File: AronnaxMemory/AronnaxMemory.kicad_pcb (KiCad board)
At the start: 6 copper layers, 152.4 x 64.8 mm, 41 parts, among them J1 Barrel_Jack_Switch, J2 Conn_02x40_Odd_Even, J3 Conn_02x18_Odd_Even, J5 I/O, J8 Conn_02x40_Odd_Even, U1 W65C22SxP, U10 ATF22V10, U11 W65C51NxP, U12 MAX232, U2 MAX232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

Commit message: All of it
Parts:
- removed J5: I/O, Connector_PinHeader_2.54mm:PinHeader_2x09_P2.54mm_Vertical
- removed U1: W65C22SxP, Package_LCC:PLCC-44_THT-Socket
- removed U11, U3: W65C51NxP, Package_LCC:PLCC-32_THT-Socket
- removed U12, U2: MAX232, Package_DIP:DIP-16_W7.62mm_Socket
- removed U6: AS6C4008-55PCN, Package_DIP:DIP-32_W15.24mm_Socket
- removed U7: AT28C256-15PU, Package_LCC:PLCC-32_THT-Socket
- removed U8: ATF22V10, Package_DIP:DIP-24_W7.62mm_Socket
- removed X2: 28MHz, Oscillator:Oscillator_DIP-8
- added C11: 100nF, Capacitor_THT:C_Disc_D3.4mm_W2.1mm_P2.50mm, F.Cu at (57.9, 113.2)
- added C12: 100nF, Capacitor_THT:C_Disc_D3.4mm_W2.1mm_P2.50mm, F.Cu at (65.8, 120.1)
- added J12: Conn_02x08_Odd_Even, Connector_PinHeader_2.54mm:PinHeader_2x08_P2.54mm_Vertical, F.Cu at (164.7, 85.7)
- added J9: VP A1-A4, Connector_PinHeader_2.54mm:PinHeader_2x04_P2.54mm_Vertical, F.Cu at (144.9, 111.3)
- J8: value Conn_02x40_Odd_Even -> Conn_02x10_Odd_Even; footprint Connector_PinHeader_2.54mm:PinHeader_2x40_P2.54mm_Vertical -> Connector_PinHeader_2.54mm:PinHeader_2x10_P2.54mm_Vertical
- moved C8 92.8 mm to (53.2, 110.9)
- moved C6 58.7 mm to (47.0, 86.4), turned to 0 degrees
- moved C10 56.9 mm to (71.9, 113.9), turned to 180 degrees
- moved J8 56.0 mm to (98.3, 107.6)
- moved U10 54.3 mm to (75.4, 122.0)
- moved C9 49.6 mm to (106.3, 115.6)
- moved U9 49.6 mm to (109.2, 123.2)
- moved C7 49.1 mm to (67.4, 100.7)
- moved C2 34.8 mm to (62.0, 107.9), turned to 90 degrees
- moved C1 20.4 mm to (39.8, 107.0), turned to 180 degrees
- moved D3 18.8 mm to (141.9, 96.6), turned to -90 degrees
- moved RN1 18.3 mm to (167.0, 93.1)
- moved C5 15.9 mm to (143.9, 93.6), turned to 180 degrees
- moved R14 15.6 mm to (144.9, 104.3)
- moved R3 15.6 mm to (169.5, 96.9)
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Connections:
- net Net-(D3-K) renamed /~{IRQV}
- J2 pad 35: R~{W} -> /R~{W}
- J2 pad 39: ~{WR} -> /~{WR}
- J3 pad 11: /AA4 -> /A4
- J3 pad 13: /AA3 -> /A3
- J3 pad 15: /AA2 -> /A2
- J3 pad 17: /AA1 -> /A1
- J8 pad 10: /AA4 -> ~{MEG6}
- J8 pad 14: ~{MEG0} -> ~{MEG8}
- J8 pad 16: ~{MEG2} -> ~{MEGA}
- J8 pad 18: ~{MEG4} -> ~{MEGC}
- J8 pad 2: ~{IRQ7} -> ~{RAM_OE}
- J8 pad 20: ~{MEG6} -> ~{MEGE}
- J8 pad 4: /AA1 -> ~{MEG0}
- J8 pad 6: /AA2 -> ~{MEG2}
- J8 pad 8: /AA3 -> ~{MEG4}
- U4 pad 2: /A1 -> /A4
- U4 pad 3: /A2 -> /A3
- U4 pad 4: /A3 -> /A2
- U4 pad 5: /A4 -> /A1
- U9 pad 1: unconnected-(U9-CLK-Pad1) -> E
- U9 pad 11: E -> /A7
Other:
- board text added: "~{CLK}"
- board text removed: "~{CLK"

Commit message: All of it p2
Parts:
- removed C10, C11, C12, C8, C9: 100nF, Capacitor_THT:C_Disc_D3.4mm_W2.1mm_P2.50mm
- removed U10, U9: ATF22V10, Package_DIP:DIP-24_W7.62mm_Socket
- added J11: Conn_02x18_Odd_Even, PCB_Edge_Connectors:PCB_Edge_36pin, B.Cu at (187.5, 100.3)
- added R13: 3.3k, Resistor_THT:R_Axial_DIN0207_L6.3mm_D2.5mm_P7.62mm_Horizontal, F.Cu at (86.2, 158.2)
- added U13: 74HC74, Package_DIP:DIP-14_W7.62mm, F.Cu at (55.9, 96.5)
- added U2: ATF22V10, Package_DIP:DIP-24_W7.62mm_Socket, F.Cu at (109.2, 119.4)
- added U3: ATF22V10, Package_DIP:DIP-24_W7.62mm_Socket, F.Cu at (76.2, 109.2)
- added U6: 74LS348, Package_DIP:DIP-16_W7.62mm_Socket, F.Cu at (142.2, 99.1)
- added U7: ATF22V10, Package_DIP:DIP-24_W7.62mm_Socket, F.Cu at (134.6, 111.8)
- added X1: 16MHz, Oscillator:Oscillator_DIP-8, F.Cu at (41.9, 118.1)
- J12: value Conn_02x08_Odd_Even -> IRQ In
- J8: value Conn_02x10_Odd_Even -> 2MB Select; footprint Connector_PinHeader_2.54mm:PinHeader_2x10_P2.54mm_Vertical -> Connector_PinHeader_2.54mm:PinHeader_2x09_P2.54mm_Vertical
- U4: value ATF22V10 -> 74AHCT32; footprint Package_DIP:DIP-24_W7.62mm_Socket -> Package_DIP:DIP-14_W7.62mm_Socket
- U5: value 74LS348 -> 74HC74; footprint Package_DIP:DIP-16_W7.62mm_Socket -> Package_DIP:DIP-14_W7.62mm
- moved C4 36.4 mm to (113.7, 92.7)
- moved U4 36.4 mm to (116.8, 97.8)
- moved C5 17.3 mm to (141.7, 76.5)
- moved D3 17.3 mm to (139.7, 79.5)
- moved R14 17.3 mm to (142.7, 87.1)
- moved R4 17.3 mm to (170.7, 79.8)
- moved J12 17.3 mm to (162.6, 68.6)
- moved R3 17.3 mm to (167.4, 79.8)
- moved R5 17.3 mm to (174.0, 79.8)
- moved RN1 17.3 mm to (164.8, 75.9)
- moved U5 17.3 mm to (146.1, 87.1)
- moved C6 11.3 mm to (41.2, 96.0)
- moved J8 9.30 mm to (99.1, 116.8)
- moved J9 8.13 mm to (144.8, 119.4)
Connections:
- net ~{RST} renamed /~{RST}
- J12 pad 10: ~{IRQ3} -> /~{IRQ3}
- J12 pad 12: ~{IRQ2} -> /~{IRQ2}
- J12 pad 14: ~{IRQ1} -> /~{IRQ1}
- J12 pad 16: ~{IRQ0} -> /~{IRQ0}
- J12 pad 2: ~{IRQ7} -> /~{IRQ7}
- J12 pad 4: ~{IRQ6} -> /~{IRQ6}
- J12 pad 6: ~{IRQ5} -> /~{IRQ5}
- J12 pad 8: ~{IRQ4} -> /~{IRQ4}
- J2 pad 11: ~{CLK_EN} -> /~{CLK_EN}
- J2 pad 15: /CLK -> unconnected-(J2-Pin_15-Pad15)
- J2 pad 17: /~{CLK} -> unconnected-(J2-Pin_17-Pad17)
- J2 pad 23: /~{ABORT} -> unconnected-(J2-Pin_23-Pad23)
- J2 pad 25: /BE -> unconnected-(J2-Pin_25-Pad25)
- J2 pad 27: /RDY_IN -> unconnected-(J2-Pin_27-Pad27)
- J2 pad 29: /~{WAI} -> unconnected-(J2-Pin_29-Pad29)
- J2 pad 31: /SYNC -> unconnected-(J2-Pin_31-Pad31)
- J2 pad 33: /VA -> unconnected-(J2-Pin_33-Pad33)
- J2 pad 41: ~{BANK0} -> /~{BANK0}
- J2 pad 43: E -> /E
- J2 pad 45: /M -> unconnected-(J2-Pin_45-Pad45)
- J2 pad 47: /X -> unconnected-(J2-Pin_47-Pad47)
- J2 pad 5: /~{MR}⎒ -> unconnected-(J2-Pin_5-Pad5)
- J2 pad 51: /~{ML} -> unconnected-(J2-Pin_51-Pad51)
- J2 pad 9: /RST -> unconnected-(J2-Pin_9-Pad9)
- J8 pad 10: ~{MEG6} -> /~{MEG8}
- J8 pad 12: ~{RAM_OE} -> /~{MEGA}
- J8 pad 14: ~{MEG8} -> /~{MEGC}
- J8 pad 16: ~{MEGA} -> /~{MEGE}
- J8 pad 18: ~{MEGC} -> ~{RAM_OE}
- J8 pad 2: ~{RAM_OE} -> /~{MEG0}
- J8 pad 4: ~{MEG0} -> /~{MEG2}
- J8 pad 6: ~{MEG2} -> /~{MEG4}
- J8 pad 8: ~{MEG4} -> /~{MEG6}
- J9 pad 2: GND -> Net-(J9-Pin_2)
- J9 pad 4: GND -> Net-(J9-Pin_2)
- J9 pad 6: GND -> Net-(J9-Pin_2)
- J9 pad 8: GND -> Net-(J9-Pin_2)
- RN1 pad 2: ~{IRQ7} -> /~{IRQ7}
- RN1 pad 3: ~{IRQ6} -> /~{IRQ6}
- RN1 pad 4: ~{IRQ5} -> /~{IRQ5}
- RN1 pad 5: ~{IRQ4} -> /~{IRQ4}
- RN1 pad 6: ~{IRQ3} -> /~{IRQ3}
- RN1 pad 7: ~{IRQ2} -> /~{IRQ2}
- RN1 pad 8: ~{IRQ1} -> /~{IRQ1}
- RN1 pad 9: ~{IRQ0} -> /~{IRQ0}
- U4 pad 1: unconnected-(U4-CLK-Pad1) -> GND
- U4 pad 10: /~{VP} -> Net-(U4-Pad10)
- U4 pad 11: unconnected-(U4-I-Pad11) -> Net-(U4-Pad10)
- U4 pad 12: GND -> /8MHz
- U4 pad 13: unconnected-(U4-I-Pad13) -> GND
- U4 pad 14: unconnected-(U4-O-Pad14) -> VCC
- U4 pad 2: /A4 -> GND
- U4 pad 3: /A3 -> unconnected-(U4-Pad3)
- U4 pad 4: /A2 -> /IOWAIT
- U4 pad 5: /A1 -> /8MHz
- U4 pad 6: unconnected-(U4-I-Pad6) -> /CLK_SRC
- U4 pad 7: /ADDEND_AA1 -> GND
- U4 pad 8: /ADDEND_AA2 -> /DCLK
- U4 pad 9: /ADDEND_AA3 -> GND
- U5 pad 1: ~{IRQ0} -> VCC
- U5 pad 10: ~{IRQ7} -> VCC
- U5 pad 11: ~{IRQ6} -> /DCLK
- U5 pad 12: ~{IRQ5} -> /STRETCH
- U5 pad 13: ~{IRQ4} -> /~{RDYRESET}
- U5 pad 14: /~{IRQV} -> VCC
- U5 pad 2: ~{IRQ1} -> /~{IOREADY}
- U5 pad 3: ~{IRQ2} -> /DCLK
- U5 pad 4: ~{IRQ3} -> /IOWAIT
- U5 pad 5: GND -> /~{RDYRESET}
- U5 pad 6: /ADDEND_AA3 -> unconnected-(U5A-~{Q}-Pad6)
- U5 pad 7: /ADDEND_AA2 -> GND
- U5 pad 8: GND -> unconnected-(U5B-~{Q}-Pad8)
- U5 pad 9: /ADDEND_AA1 -> /IOWAIT
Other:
- board size 152.4 x 64.8 mm -> 161.3 x 64.8 mm

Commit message: All of it.
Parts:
- removed D3: 1N4148, Diode_THT:D_DO-35_SOD27_P7.62mm_Horizontal
- removed R14: 10K, Resistor_THT:R_Axial_DIN0207_L6.3mm_D2.5mm_P7.62mm_Horizontal
- added D4: 1N4148, Diode_THT:D_DO-35_SOD27_P7.62mm_Horizontal, F.Cu at (51.4, 114.3)
- added R15: 10K, Resistor_THT:R_Axial_DIN0207_L6.3mm_D2.5mm_P7.62mm_Horizontal, F.Cu at (51.4, 118.1)
- moved R13 69.1 mm to (94.0, 89.5)
- moved C5 2.58 mm to (142.9, 78.8), turned to -90 degrees
- moved J12 0.64 mm to (162.6, 67.9)
- moved R3 0.64 mm to (167.4, 79.1)
- moved R4 0.64 mm to (170.7, 79.1)
- moved R5 0.64 mm to (174.0, 79.1)
- moved RN1 0.64 mm to (164.8, 75.3)
- moved U5 0.64 mm to (146.1, 86.5)
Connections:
- J11 pad 13: GND2 -> GND
- J11 pad 19: GND2 -> GND
- J11 pad 25: GND2 -> GND
- J11 pad 29: VDD -> VCC
- J11 pad 31: GND2 -> GND
- J11 pad 33: ~{IRQ} -> /~{IRQ}
- J11 pad 7: GND2 -> GND
- J11 pad 8: VDD -> VCC
- J2 pad 19: ~{IRQ} -> /~{IRQ}
- J8 pad 18: ~{RAM_OE} -> /I/O
- U2 pad 21: ~{RAM_OE} -> unconnected-(U2-O-Pad21)
- U2 pad 22: ~{ROM_OE} -> /I/O
- U3 pad 23: ~{RAM_OE} -> /I/O
- U6 pad 14: /~{IRQV} -> /~{IRQ_VALID}
- U7 pad 11: unconnected-(U7-I-Pad11) -> /E
- U7 pad 16: ~{IRQ} -> unconnected-(U7-O-Pad16)
- U7 pad 23: unconnected-(U7-O-Pad23) -> /~{IRQ_ASSERT}
- U7 pad 6: unconnected-(U7-I-Pad6) -> /~{IRQ_VALID}
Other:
- outline, holes or cut-outs redrawn

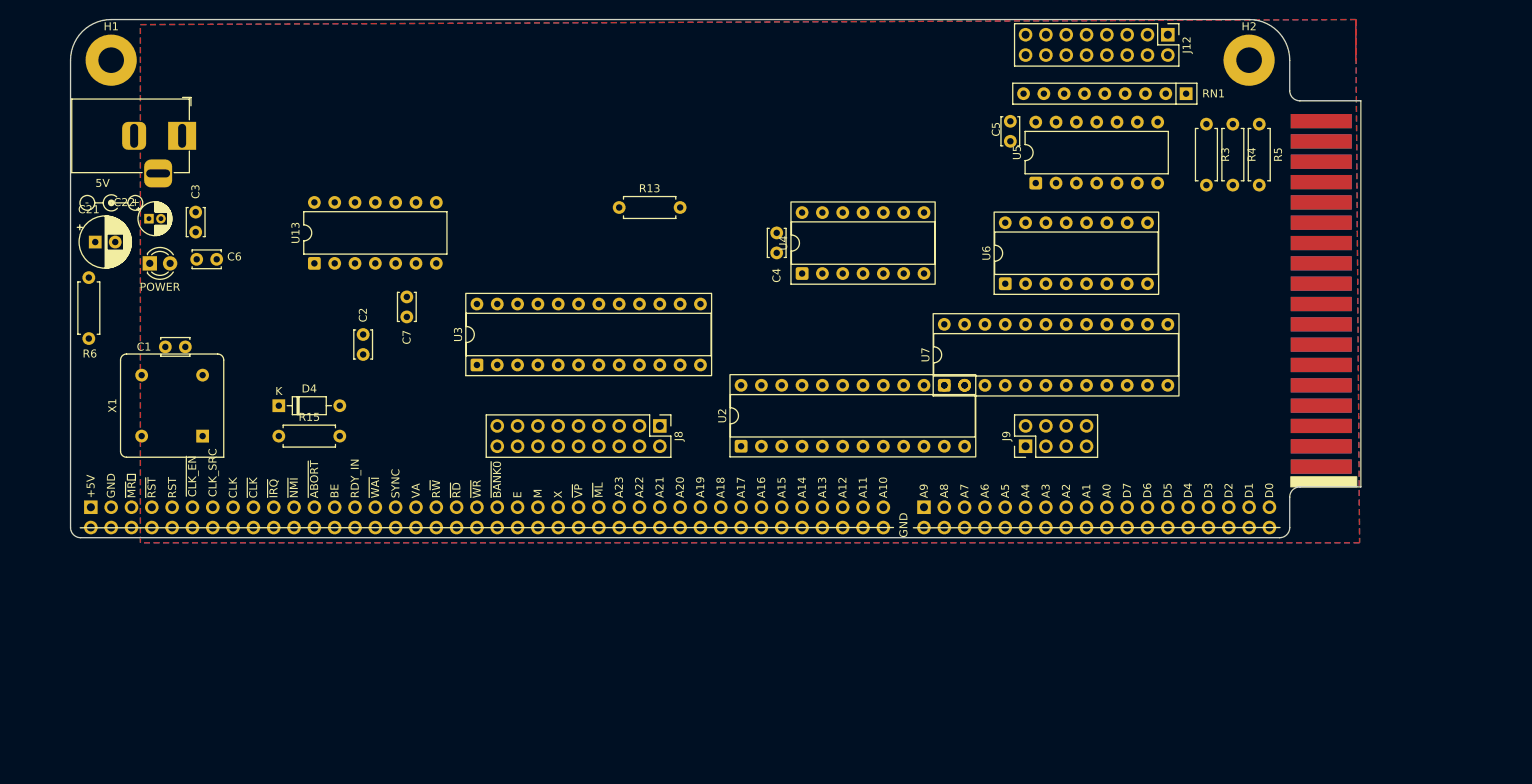
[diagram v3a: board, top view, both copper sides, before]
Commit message: Before replacing 22V10 with 4 bit adder
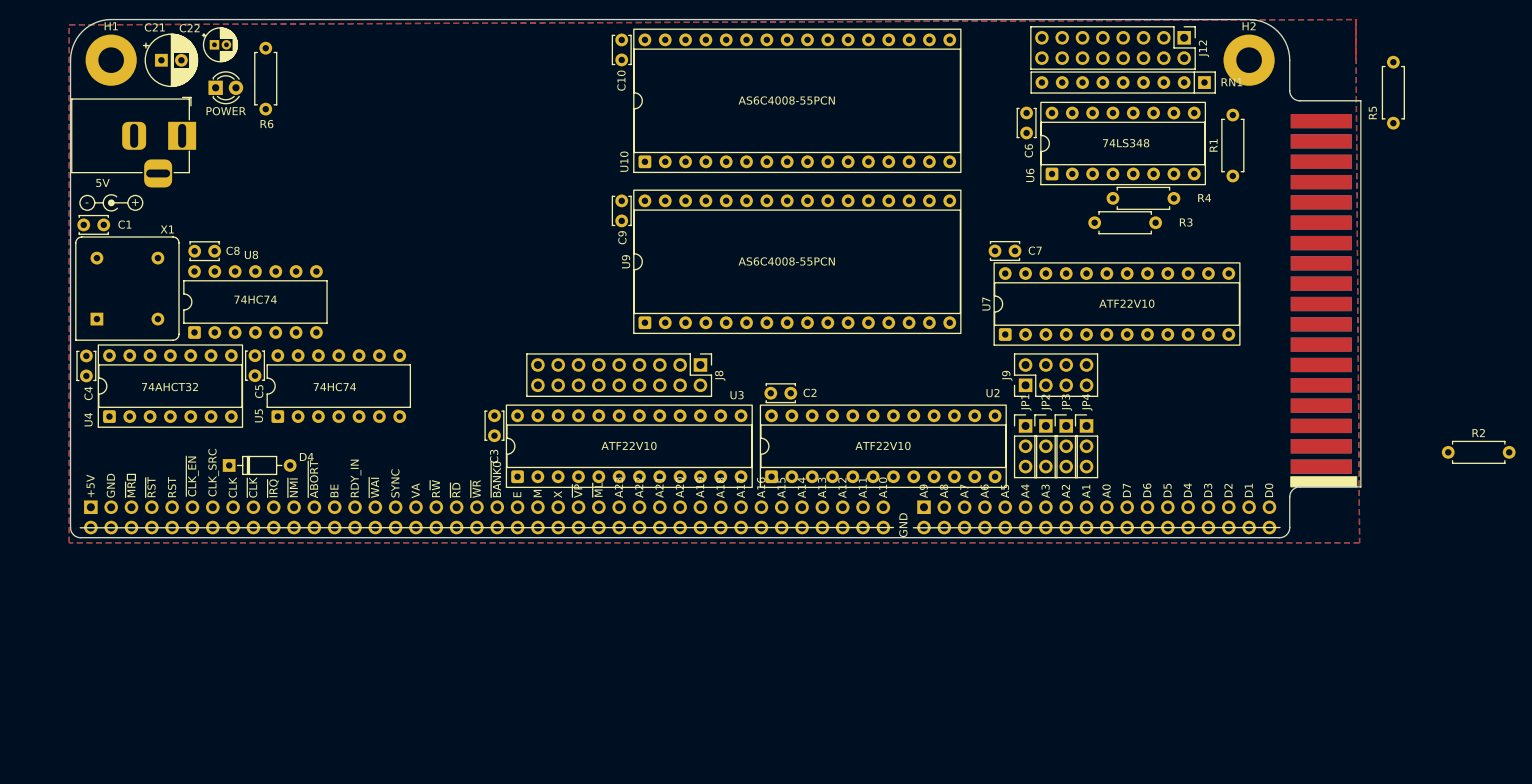
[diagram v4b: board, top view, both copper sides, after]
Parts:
- removed R13: 3.3k, Resistor_THT:R_Axial_DIN0207_L6.3mm_D2.5mm_P7.62mm_Horizontal
- removed R15: 10K, Resistor_THT:R_Axial_DIN0207_L6.3mm_D2.5mm_P7.62mm_Horizontal
- removed U13: 74HC74, Package_DIP:DIP-14_W7.62mm
- added C10: 100nF, Capacitor_THT:C_Disc_D3.4mm_W2.1mm_P2.50mm, F.Cu at (94.3, 68.6)
- added C8: 100nF, Capacitor_THT:C_Disc_D3.4mm_W2.1mm_P2.50mm, F.Cu at (40.9, 95.0)
- added C9: 100nF, Capacitor_THT:C_Disc_D3.4mm_W2.1mm_P2.50mm, F.Cu at (94.3, 88.7)
- added JP1: Jumper3_254mm, Jumper3_254mm:Jumper3_254mm, F.Cu at (144.8, 116.8)
- added JP2: Jumper3_254mm, Jumper3_254mm:Jumper3_254mm, F.Cu at (147.3, 116.8)
- added JP3: Jumper3_254mm, Jumper3_254mm:Jumper3_254mm, F.Cu at (149.9, 116.8)
- added JP4: Jumper3_254mm, Jumper3_254mm:Jumper3_254mm, F.Cu at (152.4, 116.8)
- added R1: 10K, Resistor_THT:R_Axial_DIN0207_L6.3mm_D2.5mm_P7.62mm_Horizontal, F.Cu at (170.7, 85.6)
- added R2: 10K, Resistor_THT:R_Axial_DIN0207_L6.3mm_D2.5mm_P7.62mm_Horizontal, F.Cu at (197.6, 120.1)
- added U10: AS6C4008-55PCN, Package_DIP:DIP-32_W15.24mm_Socket, F.Cu at (97.2, 83.8)
- added U8: 74HC74, Package_DIP:DIP-14_W7.62mm, F.Cu at (40.9, 105.2)
- added U9: AS6C4008-55PCN, Package_DIP:DIP-32_W15.24mm_Socket, F.Cu at (97.2, 103.9)
- J8: value 2MB Select -> RAM Select
- R4: value 10K -> 1k
- R6: value 1k -> 3.3k
- moved C6 105.3 mm to (144.9, 77.7), turned to -90 degrees
- moved U5 99.1 mm to (51.3, 115.7)
- moved C5 98.9 mm to (48.5, 108.1)
- moved U4 88.4 mm to (30.3, 115.7)
- moved C4 87.6 mm to (27.4, 108.1)
- moved C7 73.7 mm to (141.0, 95.0), turned to 0 degrees
- moved C2 51.2 mm to (112.9, 112.8), turned to 0 degrees
- moved C3 43.8 mm to (78.4, 115.6), turned to -90 degrees
- moved R6 36.2 mm to (49.8, 77.2)
- moved C21 24.2 mm to (36.8, 71.1)
- moved D1 23.4 mm to (43.5, 74.6)
- moved C22 23.2 mm to (43.4, 69.2)
- moved C1 19.8 mm to (27.1, 91.7), turned to 0 degrees
- moved X1 19.7 mm to (28.7, 103.5), turned to 0 degrees
- moved R3 18.6 mm to (153.4, 91.4), turned to 0 degrees
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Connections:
- net /~{MEG0} renamed /~{RAM_0}
- net /~{MEG2} renamed /~{RAM_1}
- net /~{MEG4} renamed /~{RAM_2}
- net /~{MEG6} renamed /~{RAM_3}
- net /~{MEG8} renamed /~{RAM_4}
- net /~{MEGA} renamed /~{RAM_5}
- net /~{MEGC} renamed /~{RAM_6}
- net /~{MEGE} renamed /~{RAM_7}
- D4 pad 1: /~{IRQ_ASSERT} -> /~{IRQ_VALID}
- J2 pad 37: ~{RD} -> /~{RD}
- J8 pad 18: /I/O -> /~{RAM_OE}
- J9 pad 1: /AA4 -> /AA1
- J9 pad 3: /AA3 -> /AA2
- J9 pad 5: /AA2 -> /AA3
- J9 pad 7: /AA1 -> /AA4
- R3 pad 2: /ADDEND_AA3 -> /ADDEND_AA1
- R4 pad 1: GND -> Net-(D1-A)
- R4 pad 2: /ADDEND_AA2 -> VCC
- R5 pad 1: GND -> VCC
- R5 pad 2: /ADDEND_AA1 -> /~{IRQ_VALID}
- R6 pad 1: Net-(D1-A) -> VCC
- R6 pad 2: VCC -> /~{CLK_EN}
- U2 pad 22: /I/O -> unconnected-(U2-O-Pad22)
- U2 pad 23: ~{I/O} -> /IO_AREA
- U3 pad 1: ~{RD} -> unconnected-(U3-CLK-Pad1)
- U3 pad 10: ~{I/O} -> /A17
- U3 pad 11: ~{ROM_OE} -> /A16
- U3 pad 2: /A23 -> /IO_AREA
- U3 pad 23: /I/O -> /~{RAM_OE}
- U3 pad 3: /A22 -> /~{RD}
- U3 pad 4: /A21 -> /A23
- U3 pad 5: /A20 -> /A22
- U3 pad 6: /A19 -> /A21
- U3 pad 7: /A18 -> /A20
- U3 pad 8: /A17 -> /A19
- U3 pad 9: /A16 -> /A18
- U5 pad 12: /STRETCH -> /IO_AREA
- U7 pad 17: /AA1 -> /AA4
- U7 pad 18: /AA2 -> /AA3
- U7 pad 19: /AA3 -> /AA2
- U7 pad 20: /AA4 -> /AA1
- U7 pad 21: /~{NMI} -> unconnected-(U7-O-Pad21)
- U7 pad 23: /~{IRQ_ASSERT} -> unconnected-(U7-O-Pad23)
- U7 pad 6: /~{IRQ_VALID} -> unconnected-(U7-I-Pad6)

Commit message: Gettin ready to publish
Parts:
- added C11: 100nF, Capacitor_THT:C_Disc_D3.4mm_W2.1mm_P2.50mm, F.Cu at (50.7, 67.4)
- added C12: 100nF, Capacitor_THT:C_Disc_D3.4mm_W2.1mm_P2.50mm, F.Cu at (50.7, 86.8)
- added U11: AS6C4008-55PCN, Package_DIP:DIP-32_W15.24mm_Socket, F.Cu at (53.6, 82.8)
- added U12: AS6C4008-55PCN, Package_DIP:DIP-32_W15.24mm_Socket, F.Cu at (53.8, 102.1)
- moved R5 144.1 mm to (53.2, 121.8)
- moved R4 113.0 mm to (43.1, 78.8), turned to -90 degrees
- moved R6 47.9 mm to (30.1, 120.9), turned to 0 degrees
- moved R2 44.0 mm to (165.4, 90.2), turned to 180 degrees
- moved U4 30.5 mm to (60.0, 122.6)
- moved C4 30.5 mm to (57.1, 115.0)
- moved U5 21.1 mm to (30.4, 118.0)
- moved C5 21.1 mm to (27.5, 110.4)
- moved U8 13.0 mm to (40.4, 92.2), turned to 0 degrees
- moved D4 9.09 mm to (50.2, 114.2), turned to -90 degrees
- moved C8 9.05 mm to (48.0, 89.3), turned to 180 degrees
- moved J9 8.03 mm to (152.4, 109.2), turned to -90 degrees
- moved JP1 7.62 mm to (152.4, 116.8)
- moved JP4 7.62 mm to (144.8, 116.8)
- moved R1 7.07 mm to (163.7, 86.4)
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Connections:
- net /~{RAM_4} renamed /~{2M_4}
- net /~{RAM_5} renamed /~{2M_5}
- net /~{RAM_6} renamed /~{2M_6}
- net /~{RAM_7} renamed /~{2M_7}
- J2 pad 53: /A23 -> /A21
- J2 pad 55: /A22 -> /A21
- J2 pad 59: /A20 -> /A21
- J2 pad 61: /A19 -> /A21
- J2 pad 63: /A18 -> /A21
- J2 pad 65: /A17 -> /A21
- J2 pad 67: /A16 -> /A21
- J2 pad 7: /~{RST} -> /~{RESET}
- J8 pad 2: /~{RAM_0} -> /~{2M_0}
- J8 pad 4: /~{RAM_1} -> /~{2M_1}
- J8 pad 6: /~{RAM_2} -> /~{2M_2}
- J8 pad 8: /~{RAM_3} -> /~{2M_3}
- J9 pad 2: Net-(J9-Pin_2) -> GND
- J9 pad 4: Net-(J9-Pin_2) -> GND
- J9 pad 6: Net-(J9-Pin_2) -> GND
- J9 pad 8: Net-(J9-Pin_2) -> GND
- JP1 pad 1: unconnected-(JP1-A-Pad1) -> /AA1
- JP1 pad 2: unconnected-(JP1-C-Pad2) -> /BA1
- JP1 pad 3: unconnected-(JP1-B-Pad3) -> /A1
- JP2 pad 1: unconnected-(JP2-A-Pad1) -> /AA2
- JP2 pad 2: unconnected-(JP2-C-Pad2) -> /BA2
- JP2 pad 3: unconnected-(JP2-B-Pad3) -> /A2
- JP3 pad 1: unconnected-(JP3-A-Pad1) -> /AA3
- JP3 pad 2: unconnected-(JP3-C-Pad2) -> /BA3
- JP3 pad 3: unconnected-(JP3-B-Pad3) -> /A3
- JP4 pad 1: unconnected-(JP4-A-Pad1) -> /AA4
- JP4 pad 2: unconnected-(JP4-C-Pad2) -> /BA4
- JP4 pad 3: unconnected-(JP4-B-Pad3) -> /A4
- R1 pad 2: /ADDEND_AA3 -> /ADDEND_AA1
- R3 pad 2: /ADDEND_AA1 -> /ADDEND_AA3
- U10 pad 1: /A18 -> /A21
- U10 pad 10: /AA2 -> /BA2
- U10 pad 11: /AA1 -> /BA1
- U10 pad 2: /A16 -> /A21
- U10 pad 30: /A17 -> /A21
- U10 pad 8: /AA4 -> /BA4
- U10 pad 9: /AA3 -> /BA3
- U2 pad 1: /E -> GND
- U2 pad 10: /A8 -> /A7
- U2 pad 11: /A7 -> /~{BANK0}
- U2 pad 13: unconnected-(U2-I-Pad13) -> /~{VP}
- U2 pad 14: unconnected-(U2-O-Pad14) -> /E
- U2 pad 2: /~{BANK0} -> /A15
- U2 pad 22: unconnected-(U2-O-Pad22) -> /A21
- U2 pad 3: /A15 -> /A14
- U2 pad 4: /A14 -> /A13
- U2 pad 5: /A13 -> /A12
- U2 pad 6: /A12 -> /A11
- U2 pad 7: /A11 -> /A10
- U2 pad 8: /A10 -> /A9
- U2 pad 9: /A9 -> /A8
- U3 pad 1: unconnected-(U3-CLK-Pad1) -> GND
- U3 pad 10: /A17 -> /A21
- U3 pad 11: /A16 -> /A21
- U3 pad 13: unconnected-(U3-I-Pad13) -> GND
- U3 pad 15: /~{RAM_0} -> /~{2M_0}
- U3 pad 16: /~{RAM_1} -> /~{2M_1}
- U3 pad 17: /~{RAM_2} -> /~{2M_2}
- U3 pad 18: /~{RAM_3} -> /~{2M_3}
- U3 pad 4: /A23 -> /A21
- U3 pad 5: /A22 -> /A21
- U3 pad 7: /A20 -> /A21
- U3 pad 8: /A19 -> /A21
- U3 pad 9: /A18 -> /A21
- U7 pad 1: unconnected-(U7-CLK-Pad1) -> GND
- U7 pad 10: /~{VP} -> GND
- U7 pad 11: /E -> GND
- U7 pad 13: unconnected-(U7-I-Pad13) -> /ADDEND_AA1
- U7 pad 14: unconnected-(U7-O-Pad14) -> /ADDEND_AA2
- U7 pad 15: unconnected-(U7-O-Pad15) -> /ADDEND_AA3
- U7 pad 16: unconnected-(U7-O-Pad16) -> /~{RAM_3}
- U7 pad 17: /AA4 -> /~{RAM_2}
- U7 pad 18: /AA3 -> /~{RAM_1}
- U7 pad 19: /AA2 -> /~{RAM_0}
- U7 pad 21: unconnected-(U7-O-Pad21) -> /AA2
- U7 pad 22: unconnected-(U7-O-Pad22) -> /AA3
- U7 pad 23: unconnected-(U7-O-Pad23) -> /AA4
- U7 pad 6: unconnected-(U7-I-Pad6) -> /A21
- U7 pad 7: /ADDEND_AA1 -> /~{2M_0}
- U7 pad 8: /ADDEND_AA2 -> /A21
- U7 pad 9: /ADDEND_AA3 -> /A21
- U9 pad 1: /A18 -> /A21
- U9 pad 10: /AA2 -> /BA2
- U9 pad 11: /AA1 -> /BA1
- U9 pad 2: /A16 -> /A21
- U9 pad 30: /A17 -> /A21
- U9 pad 8: /AA4 -> /BA4
- U9 pad 9: /AA3 -> /BA3
